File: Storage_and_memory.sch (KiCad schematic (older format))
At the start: 6 parts

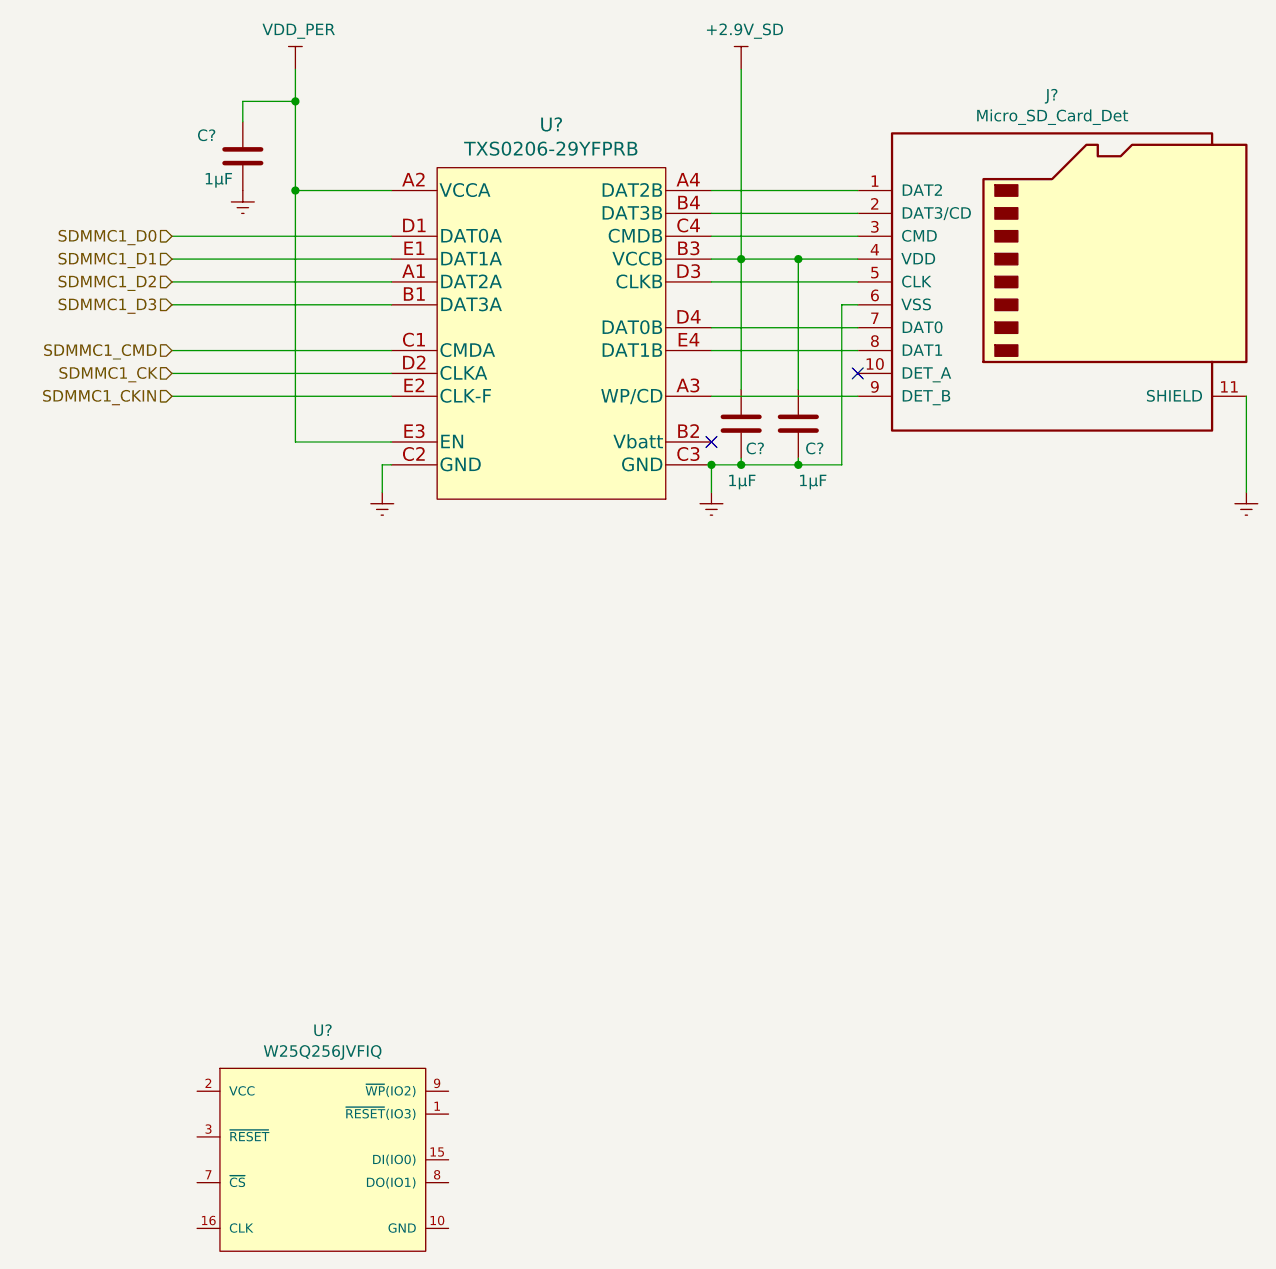
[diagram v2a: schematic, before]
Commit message: QSPI and storage sheet finished
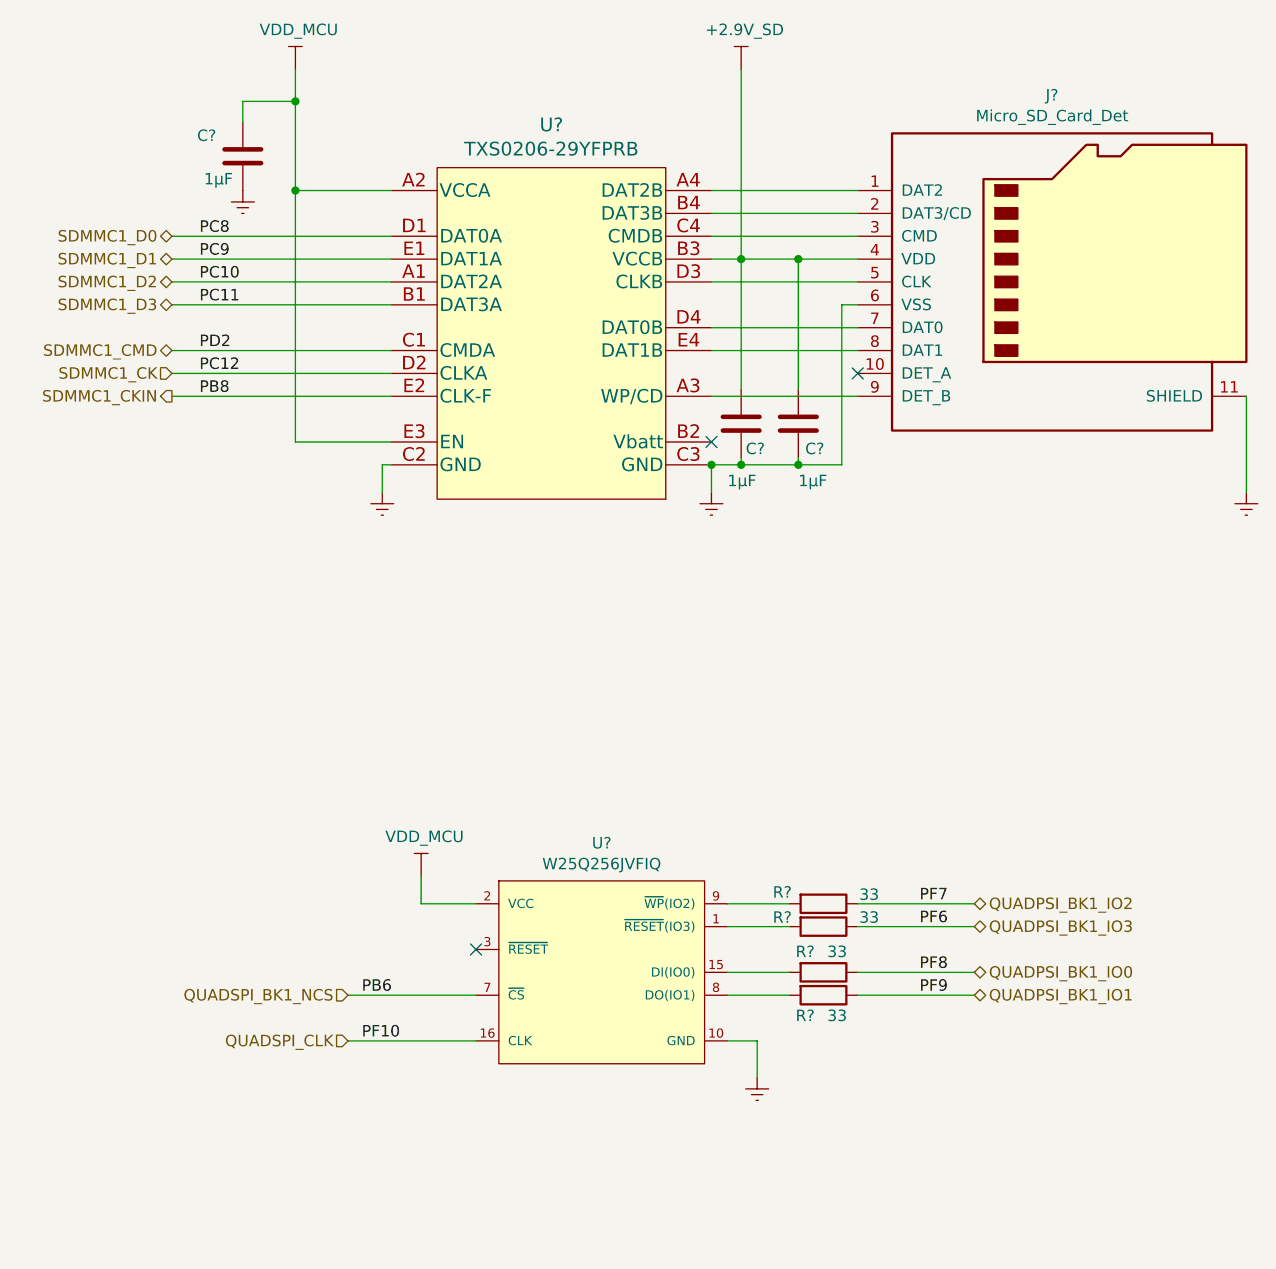
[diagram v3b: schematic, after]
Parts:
- added R? (x4): 33, Resistor_SMD:R_0805_2012Metric_Pad1.20x1.40mm_HandSolder, symbol Device:R
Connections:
- net VDD_PER is gone; now on net VDD_MCU: C?.1, U?.A2 (VCCA), U?.E3 (EN)
- net GNDREF: now also U?.10 (GND)
- net at U?.1 (~RESET~(IO3)): now also R?.2
- net at U?.15 (DI(IO0)): now also R?.2
- net QUADSPI_CLK: now reaches U?.16 (CLK)
- net VDD_MCU: now reaches U?.2 (VCC)
- net QUADSPI_BK1_NCS: now reaches U?.7 (~CS)
- net at U?.8 (DO(IO1)): now also R?.2
- net at U?.9 (~WP~(IO2)): now also R?.2
- new net QUADPSI_BK1_IO0: R?.1
- new net QUADPSI_BK1_IO1: R?.1
- new net QUADPSI_BK1_IO2: R?.1
- new net QUADPSI_BK1_IO3: R?.1
- no-connect marks 2 -> 3
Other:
- moved on the sheet: U?
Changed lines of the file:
@@
 encoding utf-8
 Sheet 6 7
-Title ""
-Date ""
-Rev ""
-Comp ""
+Title "QuadSPI Flash and SD Card storage"
+Date "2021-05-08"
+Rev "0.1"
+Comp "SVIELCOM"
 Comment1 ""
 Comment2 ""
@@
 L Схема-и-печатная-плата-rescue:W25Q256JVFIQ-Memory_Flash U?
 U 1 1 60D8B67A
-P 3050 5530
-F 0 "U?" H 3600 5795 50  0000 C CNN
-F 1 "W25Q256JVFIQ" H 3600 5704 50  0000 C CNN
-F 2 "Package_SO:SOIC-16W_7.5x10.3mm_P1.27mm" H 3050 5930 50  0001 L CNN
-F 3 "http://www.winbond.com/resource-files/w25q256jv%20spi%20reve%2002102017.pdf" H 3050 6030 50  0001 L CNN
-F 4 "IC" H 3050 6130 50  0001 L CNN "category"
-F 5 "IC FLASH 256MBIT 104MHZ 16WSOIC" H 3050 6230 50  0001 L CNN "digikey description"
-F 6 "Winbond" H 3050 6730 50  0001 L CNN "manufacturer"
-F 7 "yes" H 3050 6930 50  0001 L CNN "rohs"
-F 8 "+85°C" H 3050 7030 50  0001 L CNN "temperature range high"
-F 9 "-40°C" H 3050 7130 50  0001 L CNN "temperature range low"
-	1    3050 5530
+P 4270 4710
+F 0 "U?" H 4820 4975 50  0000 C CNN
+F 1 "W25Q256JVFIQ" H 4820 4884 50  0000 C CNN
+F 2 "Package_SO:SOIC-16W_7.5x10.3mm_P1.27mm" H 4270 5110 50  0001 L CNN
+F 3 "http://www.winbond.com/resource-files/w25q256jv%20spi%20reve%2002102017.pdf" H 4270 5210 50  0001 L CNN
+F 4 "IC" H 4270 5310 50  0001 L CNN "category"
+F 5 "IC FLASH 256MBIT 104MHZ 16WSOIC" H 4270 5410 50  0001 L CNN "digikey description"
+F 6 "Winbond" H 4270 5910 50  0001 L CNN "manufacturer"
+F 7 "yes" H 4270 6110 50  0001 L CNN "rohs"
+F 8 "+85°C" H 4270 6210 50  0001 L CNN "temperature range high"
+F 9 "-40°C" H 4270 6310 50  0001 L CNN "temperature range low"
+	1    4270 4710
 	1    0    0    -1
 $EndComp
@@
 Wire Wire Line
 	5680 1890 5940 1890
-$Comp
-L SVIELCOM_Library:VDD_PER #PWR?
-U 1 1 60995939
-P 3480 1060
-F 0 "#PWR?" H 3480 910 50  0001 C CNN
-F 1 "VDD_PER" H 3495 1233 50  0000 C CNN
-F 2 "" H 3480 1060 50  0001 C CNN
-F 3 "" H 3480 1060 50  0001 C CNN
-	1    3480 1060
-	1    0    0    -1
-$EndComp
 Wire Wire Line
 	3480 1060 3480 1200
@@
 Wire Wire Line
 	2940 2490 3900 2490
-Text HLabel 2940 1790 0    50   Input ~ 0
+Text HLabel 2940 1790 0    50   BiDi ~ 0
 SDMMC1_D0
-Text HLabel 2940 1890 0    50   Input ~ 0
+Text HLabel 2940 1890 0    50   BiDi ~ 0
 SDMMC1_D1
-Text HLabel 2940 1990 0    50   Input ~ 0
+Text HLabel 2940 1990 0    50   BiDi ~ 0
 SDMMC1_D2
-Text HLabel 2940 2090 0    50   Input ~ 0
+Text HLabel 2940 2090 0    50   BiDi ~ 0
 SDMMC1_D3
-Text HLabel 2940 2290 0    50   Input ~ 0
+Text HLabel 2940 2290 0    50   BiDi ~ 0
 SDMMC1_CMD
 Text HLabel 2940 2390 0    50   Input ~ 0
 SDMMC1_CK
-Text HLabel 2940 2490 0    50   Input ~ 0
+Text HLabel 2940 2490 0    50   Output ~ 0
 SDMMC1_CKIN
+Text Label 3060 1790 0    50   ~ 0
+PC8
+Text Label 3060 1890 0    50   ~ 0
+PC9
+Text Label 3060 1990 0    50   ~ 0
+PC10
+Text Label 3060 2090 0    50   ~ 0
+PC11
+Text Label 3060 2290 0    50   ~ 0
+PD2
+Text Label 3060 2390 0    50   ~ 0
+PC12
+Text Label 3060 2490 0    50   ~ 0
+PB8
+$Comp
+L SVIELCOM_Library:VDD_MCU #PWR?
+U 1 1 60A156B1
+P 3480 1060
+F 0 "#PWR?" H 3480 910 50  0001 C CNN
+F 1 "VDD_MCU" H 3495 1233 50  0000 C CNN
+F 2 "" H 3480 1060 50  0001 C CNN
+F 3 "" H 3480 1060 50  0001 C CNN
+	1    3480 1060
+	1    0    0    -1
+$EndComp
+$Comp
+L SVIELCOM_Library:VDD_MCU #PWR?
+U 1 1 60A15E6C
+P 4030 4590
+F 0 "#PWR?" H 4030 4440 50  0001 C CNN
+F 1 "VDD_MCU" H 4045 4763 50  0000 C CNN
+F 2 "" H 4030 4590 50  0001 C CNN
+F 3 "" H 4030 4590 50  0001 C CNN
+	1    4030 4590
+	1    0    0    -1
+$EndComp
+Wire Wire Line
+	4030 4590 4030 4710
+Wire Wire Line
+	4030 4710 4270 4710
+$Comp
+L power:GNDREF #PWR?
+U 1 1 60A17165
+P 5500 5470
+AR Path="/60A17165" Ref="#PWR?"  Part="1"
+AR Path="/60A03F8A/60A17165" Ref="#PWR?"  Part="1"
+AR Path="/60D8A641/60A17165" Ref="#PWR?"  Part="1"
+F 0 "#PWR?" H 5500 5220 50  0001 C CNN
+F 1 "GNDREF" V 5505 5342 50  0001 R CNN
+F 2 "" H 5500 5470 50  0001 C CNN
+F 3 "" H 5500 5470 50  0001 C CNN
+	1    5500 5470
+	1    0    0    -1
+$EndComp
+Wire Wire Line
+	5370 5310 5500 5310
+Wire Wire Line
+	5500 5310 5500 5470
+$Comp
+L Device:R R?
+U 1 1 60A1C3E5
+P 5790 4710
+AR Path="/60A1C3E5" Ref="R?"  Part="1"
+AR Path="/60A03F8A/60A1C3E5" Ref="R?"  Part="1"
+AR Path="/60D8A641/60A1C3E5" Ref="R?"  Part="1"
+F 0 "R?" V 5740 4530 50  0000 C CNN
+F 1 "33" V 5750 4910 50  0000 C CNN
+F 2 "Resistor_SMD:R_0805_2012Metric_Pad1.20x1.40mm_HandSolder" V 5720 4710 50  0001 C CNN
+F 3 "~" H 5790 4710 50  0001 C CNN
+	1    5790 4710
+	0    1    1    0
+$EndComp
+Wire Wire Line
+	5370 4710 5640 4710
+$Comp
+L Device:R R?
+U 1 1 60A1DE64
+P 5790 4810
+AR Path="/60A1DE64" Ref="R?"  Part="1"
+AR Path="/60A03F8A/60A1DE64" Ref="R?"  Part="1"
+AR Path="/60D8A641/60A1DE64" Ref="R?"  Part="1"
+F 0 "R?" V 5750 4630 50  0000 C CNN
+F 1 "33" V 5750 5010 50  0000 C CNN
+F 2 "Resistor_SMD:R_0805_2012Metric_Pad1.20x1.40mm_HandSolder" V 5720 4810 50  0001 C CNN
+F 3 "~" H 5790 4810 50  0001 C CNN
+	1    5790 4810
+	0    1    1    0
+$EndComp
+Wire Wire Line
+	5370 4810 5640 4810
+$Comp
+L Device:R R?
+U 1 1 60A1EB77
+P 5790 5010
+AR Path="/60A1EB77" Ref="R?"  Part="1"
+AR Path="/60A03F8A/60A1EB77" Ref="R?"  Part="1"
+AR Path="/60D8A641/60A1EB77" Ref="R?"  Part="1"
+F 0 "R?" V 5700 4930 50  0000 C CNN
+F 1 "33" V 5700 5070 50  0000 C CNN
+F 2 "Resistor_SMD:R_0805_2012Metric_Pad1.20x1.40mm_HandSolder" V 5720 5010 50  0001 C CNN
+F 3 "~" H 5790 5010 50  0001 C CNN
+	1    5790 5010
+	0    1    1    0
+$EndComp
+Wire Wire Line
+	5370 5010 5640 5010
+$Comp
+L Device:R R?
+U 1 1 60A1F94D
+P 5790 5110
+AR Path="/60A1F94D" Ref="R?"  Part="1"
+AR Path="/60A03F8A/60A1F94D" Ref="R?"  Part="1"
+AR Path="/60D8A641/60A1F94D" Ref="R?"  Part="1"
+F 0 "R?" V 5880 5030 50  0000 C CNN
+F 1 "33" V 5880 5170 50  0000 C CNN
+F 2 "Resistor_SMD:R_0805_2012Metric_Pad1.20x1.40mm_HandSolder" V 5720 5110 50  0001 C CNN
+F 3 "~" H 5790 5110 50  0001 C CNN
+	1    5790 5110
+	0    1    1    0
+$EndComp
+Wire Wire Line
+	5370 5110 5640 5110
+NoConn ~ 4270 4910
+Wire Wire Line
+	3710 5110 4270 5110
+Wire Wire Line
+	3710 5310 4270 5310
+Text HLabel 3710 5110 0    50   Input ~ 0
+QUADSPI_BK1_NCS
+Text HLabel 3710 5310 0    50   Input ~ 0
+QUADSPI_CLK
+Wire Wire Line
+	6450 4710 5940 4710
+Wire Wire Line
+	6450 4810 5940 4810
+Wire Wire Line
+	6450 5010 5940 5010
+Wire Wire Line
+	6450 5110 5940 5110
+Text HLabel 6450 4710 2    50   BiDi ~ 0
+QUADPSI_BK1_IO2
+Text HLabel 6450 4810 2    50   BiDi ~ 0
+QUADPSI_BK1_IO3
+Text HLabel 6450 5010 2    50   BiDi ~ 0
+QUADPSI_BK1_IO0
+Text HLabel 6450 5110 2    50   BiDi ~ 0
+QUADPSI_BK1_IO1
+Text Label 6210 4710 0    50   ~ 0
+PF7
+Text Label 6210 4810 0    50   ~ 0
+PF6
+Text Label 6210 5010 0    50   ~ 0
+PF8
+Text Label 6210 5110 0    50   ~ 0
+PF9
+Text Label 3770 5310 0    50   ~ 0
+PF10
+Text Label 3770 5110 0    50   ~ 0
+PB6
 $EndSCHEMATC
